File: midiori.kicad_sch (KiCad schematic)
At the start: 85 parts, among them J1 midiori-rescue_x68000_expansi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, J2 Conn_ARM_JTAG_SWD_10, J3 AudioJack3, J4 Mini-DIN-5, J5 AudioJack3, J6 AudioJack3, J7 Conn_01x06, J8 AudioJack3, J9 Mini-DIN-5, U1 74LCX07, U10 ICE40HX1K-TQ144, U11 AP2205K-3.3, U12 AK4432, U13 TL074, U14 AP2205K-3.3, U15 TL072, U16 74LCX07, U17 H11L1, U18 SN74LVC245APW, U2 AT25SF081-SSHD-X, U3 AP2127K-1.2, U4 SN74LVC245APW, U5 SN74LVC245APW, U6 SN74LVC245APW, U7 SN74LVC245APW, U8 SN74LVC245APW, U9 SN74LVC245APW, X1 16MHz, X2 24.576MHz

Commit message: drc fixes
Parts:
- H1, H2: value MountingHole -> MountingHole_Pad; symbol Mechanical:MountingHole -> Mechanical:MountingHole_Pad
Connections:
- net GND: now also H1.1, H2.1
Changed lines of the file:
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@@
 	)
 	(symbol
-		(lib_id "Mechanical:MountingHole")
+		(lib_id "Mechanical:MountingHole_Pad")
 		(at 260.35 254 0)
 		(unit 1)
-		(exclude_from_sim no)
+		(exclude_from_sim yes)
 		(in_bom no)
 		(on_board yes)
@@
 			)
 		)
-		(property "Value" "MountingHole"
-			(at 262.89 255.143 0)
+		(property "Value" "MountingHole_Pad"
+			(at 260.35 249.555 0)
 			(effects
 				(font
 					(size 1.27 1.27)
 				)
-				(justify left)
 			)
 		)
@@
 			)
 		)
-		(property "Description" ""
+		(property "Description" "Mounting Hole with connection"
 			(at 260.35 254 0)
 			(effects
@@
 			)
 		)
+		(pin "1"
+		)
 		(instances
 			(project ""
@@
 	)
 	(symbol
-		(lib_id "Mechanical:MountingHole")
+		(lib_id "Mechanical:MountingHole_Pad")
 		(at 285.75 254 0)
 		(unit 1)
-		(exclude_from_sim no)
+		(exclude_from_sim yes)
 		(in_bom no)
 		(on_board yes)
@@
 			)
 		)
-		(property "Value" "MountingHole"
-			(at 288.29 255.143 0)
+		(property "Value" "MountingHole_Pad"
+			(at 285.75 249.555 0)
 			(effects
 				(font
 					(size 1.27 1.27)
 				)
-				(justify left)
 			)
 		)
@@
 			)
 		)
-		(property "Description" ""
+		(property "Description" "Mounting Hole with connection"
 			(at 285.75 254 0)
 			(effects
@@
 			)
 		)
+		(pin "1"
+		)
 		(instances
 			(project ""
@@
 	(symbol
 		(lib_id "power:GND")
+		(at 260.35 256.54 0)
+		(unit 1)
+		(exclude_from_sim no)
+		(in_bom yes)
+		(on_board yes)
+		(dnp no)
+		(fields_autoplaced yes)
+		(property "Reference" "#PWR041"
+			(at 260.35 262.89 0)
+			(effects
+				(font
+					(size 1.27 1.27)
+				)
+				(hide yes)
+			)
+		)
+		(property "Value" "GND"
+			(at 260.35 260.6731 0)
+			(effects
+				(font
+					(size 1.27 1.27)
+				)
+			)
+		)
+		(property "Footprint" ""
+			(at 260.35 256.54 0)
+			(effects
+				(font
+					(size 1.27 1.27)
+				)
+				(hide yes)
+			)
+		)
+		(property "Datasheet" ""
+			(at 260.35 256.54 0)
+			(effects
+				(font
+					(size 1.27 1.27)
+				)
+				(hide yes)
+			)
+		)
+		(property "Description" "Power symbol creates a global label with name \"GND\" , ground"
+			(at 260.35 256.54 0)
+			(effects
+				(font
+					(size 1.27 1.27)
+				)
+				(hide yes)
+			)
+		)
+		(pin "1"
+		)
+		(instances
+			(project "midiori"
+				(path "/89a089da-4491-480f-b113-8450a227c3da"
+					(reference "#PWR041")
+					(unit 1)
+				)
+			)
+		)
+	)
+	(symbol
+		(lib_id "power:GND")
 		(at 292.1 203.2 0)
 		(unit 1)
@@
 				)
 			)
+		)
+	)
+	(symbol
+		(lib_id "power:GND")
+		(at 285.75 256.54 0)
+		(unit 1)
+		(exclude_from_sim no)
+		(in_bom yes)
+		(on_board yes)
+		(dnp no)
+		(fields_autoplaced yes)
+		(property "Reference" "#PWR044"
+			(at 285.75 262.89 0)
+			(effects
+				(font
+					(size 1.27 1.27)
+				)
+				(hide yes)
+			)
+		)
+		(property "Value" "GND"
+			(at 285.75 260.6731 0)
+			(effects
+				(font
+					(size 1.27 1.27)
+				)
+			)
+		)
+		(property "Footprint" ""
+			(at 285.75 256.54 0)
+			(effects
+				(font
+					(size 1.27 1.27)
+				)
+				(hide yes)
+			)
+		)
+		(property "Datasheet" ""
+			(at 285.75 256.54 0)
+			(effects
+				(font
+					(size 1.27 1.27)
+				)
+				(hide yes)
+			)
+		)
+		(property "Description" "Power symbol creates a global label with name \"GND\" , ground"
+			(at 285.75 256.54 0)
+			(effects
+				(font
+					(size 1.27 1.27)
+				)
+				(hide yes)
+			)
+		)
+		(pin "1"
+		)
+		(instances
+			(project "midiori"
+				(path "/89a089da-4491-480f-b113-8450a227c3da"
+					(reference "#PWR044")
+					(unit 1)
+				)
+			)

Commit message: some extra test pads
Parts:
- added C15, C38, C39: 0.1uF, Capacitor_SMD:C_0805_2012Metric, symbol Device:C
- added R17: 10k, Resistor_SMD:R_0805_2012Metric, symbol Device:R
- added TP1, TP2: TestPoint, TestPoint:TestPoint_THTPad_1.0x1.0mm_Drill0.5mm, symbol Connector:TestPoint
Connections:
- net +3V3: now also C15.1, C38.1, C39.1, R17.1
- net GND: now also C15.2, C38.2, C39.2
- net data_dir: now also R17.2
- net CBSEL0: now reaches U10.63 (IOB_42_CBSEL0)
- net CBSEL0: now also TP1.1
- net CBSEL1: now reaches U10.64 (IOB_43_CBSEL1)
- net CBSEL1: now also TP2.1
- no-connect marks 52 -> 50

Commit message: v3.0
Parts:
- J1, TP1, TP2: now left out of the parts list
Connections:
- net at J8.T, J9.5: now also U17.2; no longer R15.2
- net at J8.R, J9.4: now also R15.2; no longer U17.2
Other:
- moved on the sheet: J8
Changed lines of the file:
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@@
 	)
 	(junction
+		(at 379.73 34.29)
+		(diameter 0)
+		(color 0 0 0 0)
+	)
+	(junction
 		(at 386.08 146.05)
 		(diameter 0)
@@
 	)
 	(junction
-		(at 377.19 36.83)
+		(at 275.59 104.14)
 		(diameter 0)
 		(color 0 0 0 0)
 	)
 	(junction
-		(at 275.59 104.14)
+		(at 381 36.83)
 		(diameter 0)
 		(color 0 0 0 0)
@@
 	)
 	(junction
-		(at 373.38 39.37)
-		(diameter 0)
-		(color 0 0 0 0)
-	)
-	(junction
 		(at 285.75 26.67)
 		(diameter 0)
@@
 	)
 	(no_connect
-		(at 377.19 41.91)
+		(at 383.54 39.37)
 	)
 	(no_connect
@@
 	(wire
 		(pts
+			(xy 377.19 36.83) (xy 381 36.83)
+		)
+		(stroke
+			(width 0)
+			(type default)
+		)
+	)
+	(wire
+		(pts
 			(xy 234.95 200.66) (xy 234.95 196.85)
 		)
@@
 	(wire
 		(pts
-			(xy 31.75 128.27) (xy 31.75 130.81)
+			(xy 374.65 27.94) (xy 374.65 21.59)
 		)
 		(stroke
@@
 	(wire
 		(pts
-			(xy 205.74 53.34) (xy 208.28 53.34)
+			(xy 31.75 128.27) (xy 31.75 130.81)
 		)
 		(stroke
@@
 	(wire
 		(pts
-			(xy 290.83 140.97) (xy 290.83 133.35)
+			(xy 205.74 53.34) (xy 208.28 53.34)
 		)
 		(stroke
@@
 	(wire
 		(pts
-			(xy 226.06 118.11) (xy 228.6 118.11)
+			(xy 290.83 140.97) (xy 290.83 133.35)
 		)
 		(stroke
@@
 	(wire
 		(pts
-			(xy 370.84 39.37) (xy 373.38 39.37)
+			(xy 226.06 118.11) (xy 228.6 118.11)
 		)
 		(stroke
@@
 	(wire
 		(pts
-			(xy 393.7 21.59) (xy 405.13 21.59)
-		)
-		(stroke
-			(width 0)
-			(type default)
-		)
-	)
-	(wire
-		(pts
 			(xy 233.68 26.67) (xy 245.11 26.67)
 		)
@@
 	(wire
 		(pts
+			(xy 383.54 34.29) (xy 379.73 34.29)
+		)
+		(stroke
+			(width 0)
+			(type default)
+		)
+	)
+	(wire
+		(pts
 			(xy 153.67 58.42) (xy 153.67 36.83)
 		)
@@
 	(wire
 		(pts
+			(xy 374.65 21.59) (xy 378.46 21.59)
+		)
+		(stroke
+			(width 0)
+			(type default)
+		)
+	)
+	(wire
+		(pts
 			(xy 248.92 212.09) (xy 234.95 212.09)
 		)
@@
 	(wire
 		(pts
+			(xy 379.73 34.29) (xy 379.73 27.94)
+		)
+		(stroke
+			(width 0)
+			(type default)
+		)
+	)
+	(wire
+		(pts
 			(xy 275.59 140.97) (xy 290.83 140.97)
 		)
@@
 	(wire
 		(pts
+			(xy 407.67 21.59) (xy 407.67 48.26)
+		)
+		(stroke
+			(width 0)
+			(type default)
+		)
+	)
+	(wire
+		(pts
 			(xy 118.11 30.48) (xy 118.11 27.94)
 		)
@@
 	(wire
 		(pts
-			(xy 405.13 49.53) (xy 373.38 49.53)
-		)
-		(stroke
-			(width 0)
-			(type default)
-		)
-	)
-	(wire
-		(pts
 			(xy 87.63 129.54) (xy 92.71 129.54)
 		)
@@
 	(wire
 		(pts
-			(xy 377.19 21.59) (xy 378.46 21.59)
+			(xy 349.25 200.66) (xy 349.25 185.42)
 		)
 		(stroke
@@
 	(wire
 		(pts
-			(xy 349.25 200.66) (xy 349.25 185.42)
+			(xy 379.73 34.29) (xy 379.73 39.37)
 		)
 		(stroke
@@
 	(wire
 		(pts
+			(xy 407.67 48.26) (xy 381 48.26)
+		)
+		(stroke
+			(width 0)
+			(type default)
+		)
+	)
+	(wire
+		(pts
 			(xy 308.61 198.12) (xy 313.69 198.12)
 		)
@@
 	(wire
 		(pts
+			(xy 381 36.83) (xy 383.54 36.83)
+		)
+		(stroke
+			(width 0)
+			(type default)
+		)
+	)
+	(wire
+		(pts
 			(xy 256.54 19.05) (xy 267.97 19.05)
 		)
@@
 	(wire
 		(pts
+			(xy 379.73 27.94) (xy 374.65 27.94)
+		)
+		(stroke
+			(width 0)
+			(type default)
+		)
+	)
+	(wire
+		(pts
 			(xy 25.4 87.63) (xy 25.4 85.09)
 		)
@@
 	(wire
 		(pts
-			(xy 373.38 39.37) (xy 377.19 39.37)
+			(xy 370.84 39.37) (xy 379.73 39.37)
 		)
 		(stroke
@@
 	(wire
 		(pts
-			(xy 295.91 123.19) (xy 280.67 123.19)
+			(xy 393.7 21.59) (xy 407.67 21.59)
 		)
 		(stroke
@@
 	(wire
 		(pts
-			(xy 195.58 240.03) (xy 200.66 240.03)
+			(xy 295.91 123.19) (xy 280.67 123.19)
 		)
 		(stroke
@@
 	(wire
 		(pts
-			(xy 151.13 53.34) (xy 151.13 34.29)
+			(xy 195.58 240.03) (xy 200.66 240.03)
 		)
 		(stroke
@@
 	(wire
 		(pts
-			(xy 351.79 58.42) (xy 360.68 58.42)
+			(xy 151.13 53.34) (xy 151.13 34.29)
 		)
 		(stroke
@@
 	(wire
 		(pts
-			(xy 403.86 205.74) (xy 396.24 205.74)
+			(xy 351.79 58.42) (xy 360.68 58.42)
 		)
 		(stroke
@@
 	(wire
 		(pts
-			(xy 360.68 146.05) (xy 360.68 156.21)
+			(xy 403.86 205.74) (xy 396.24 205.74)
 		)
 		(stroke
@@
 	(wire
 		(pts
-			(xy 405.13 21.59) (xy 405.13 49.53)
+			(xy 360.68 146.05) (xy 360.68 156.21)
 		)
 		(stroke
@@
 	(wire
 		(pts
-			(xy 377.19 36.83) (xy 377.19 21.59)
-		)
-		(stroke
-			(width 0)
-			(type default)
-		)
-	)
-	(wire
-		(pts
 			(xy 168.91 247.65) (xy 168.91 256.54)
 		)
@@
 	(wire
 		(pts
+			(xy 381 36.83) (xy 381 48.26)
+		)
+		(stroke
+			(width 0)
+			(type default)
+		)
+	)
+	(wire
+		(pts
 			(xy 281.94 53.34) (xy 293.37 53.34)
 		)
@@
 	(wire
 		(pts
-			(xy 373.38 39.37) (xy 373.38 49.53)
-		)
-		(stroke
-			(width 0)
-			(type default)
-		)
-	)
-	(wire
-		(pts
 			(xy 146.05 240.03) (xy 148.59 240.03)
 		)
@@
 		(unit 1)
 		(exclude_from_sim no)
-		(in_bom yes)
+		(in_bom no)
 		(on_board yes)
 		(dnp no)
@@
 		(unit 1)
 		(exclude_from_sim no)
-		(in_bom yes)
+		(in_bom no)
 		(on_board yes)
 		(dnp no)
@@
 		(unit 1)
 		(exclude_from_sim no)
-		(in_bom yes)
+		(in_bom no)
 		(on_board yes)
 		(dnp no)
@@
 	(symbol
 		(lib_id "Connector_Audio:AudioJack3")
-		(at 382.27 39.37 180)
+		(at 388.62 36.83 180)
 		(unit 1)
 		(exclude_from_sim no)
@@
 		(fields_autoplaced yes)
 		(property "Reference" "J8"
-			(at 389.382 37.5228 0)
+			(at 395.732 34.9828 0)
 			(effects
 				(font
@@
 		)
 		(property "Value" "AudioJack3"
-			(at 389.382 39.9471 0)
+			(at 395.732 37.4071 0)
 			(effects
 				(font
@@
 		)
 		(property "Footprint" "Connector_Audio:Jack_3.5mm_CUI_SJ1-3533NG_Horizontal"
-			(at 382.27 39.37 0)
+			(at 388.62 36.83 0)
 			(effects
 				(font
@@
 		)
 		(property "Datasheet" "~"
-			(at 382.27 39.37 0)
+			(at 388.62 36.83 0)
 			(effects
 				(font
@@
 		)
 		(property "Description" "Audio Jack, 3 Poles (Stereo / TRS)"
-			(at 382.27 39.37 0)
+			(at 388.62 36.83 0)
 			(effects
 				(font

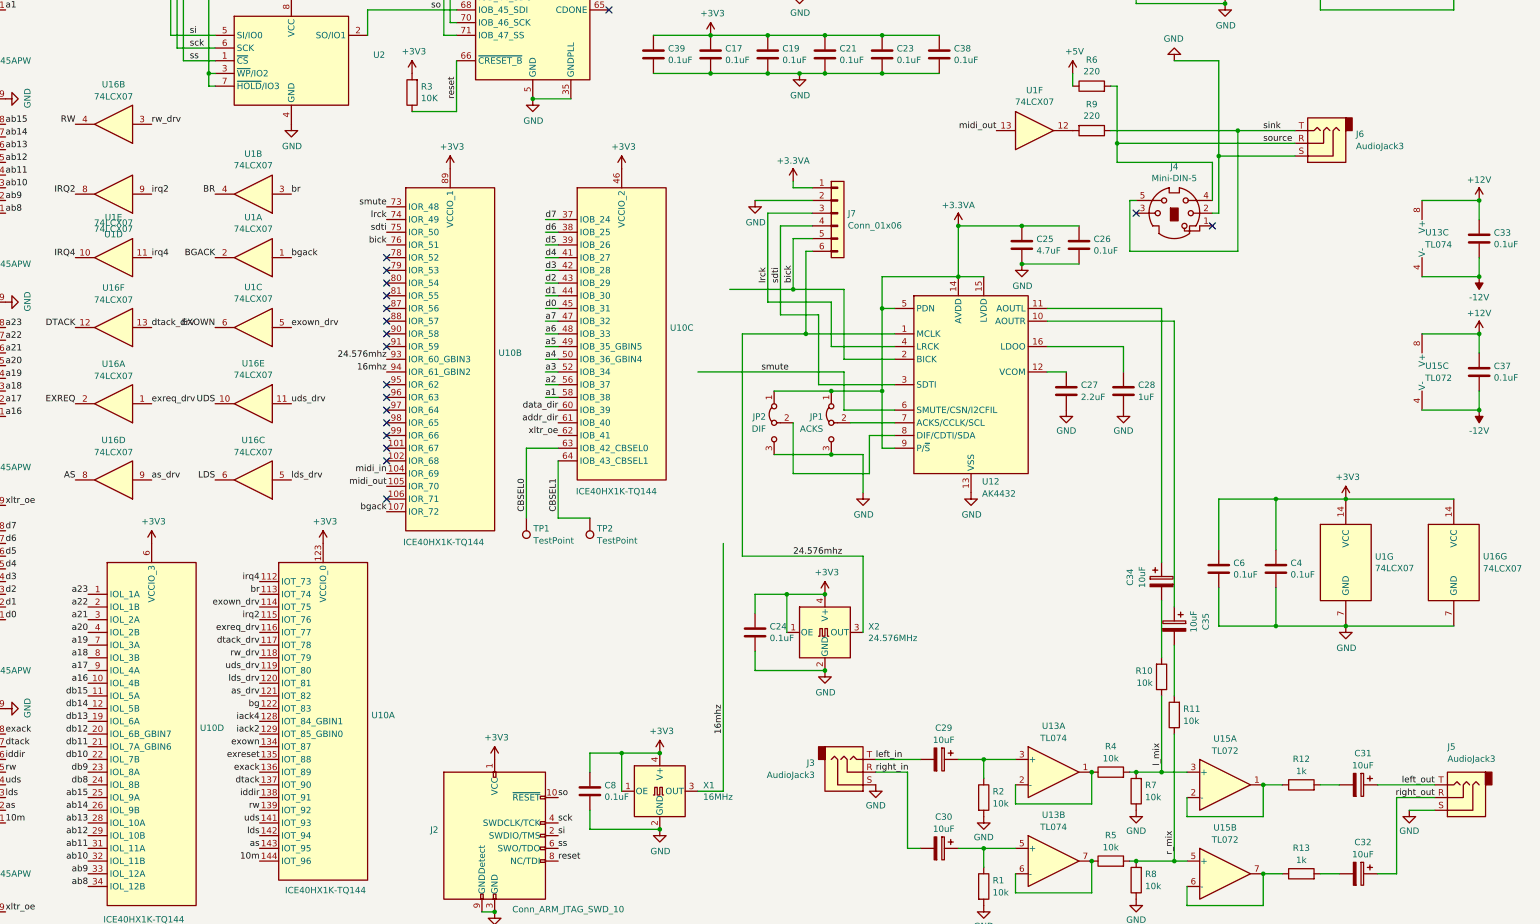
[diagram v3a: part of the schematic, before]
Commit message: add bom
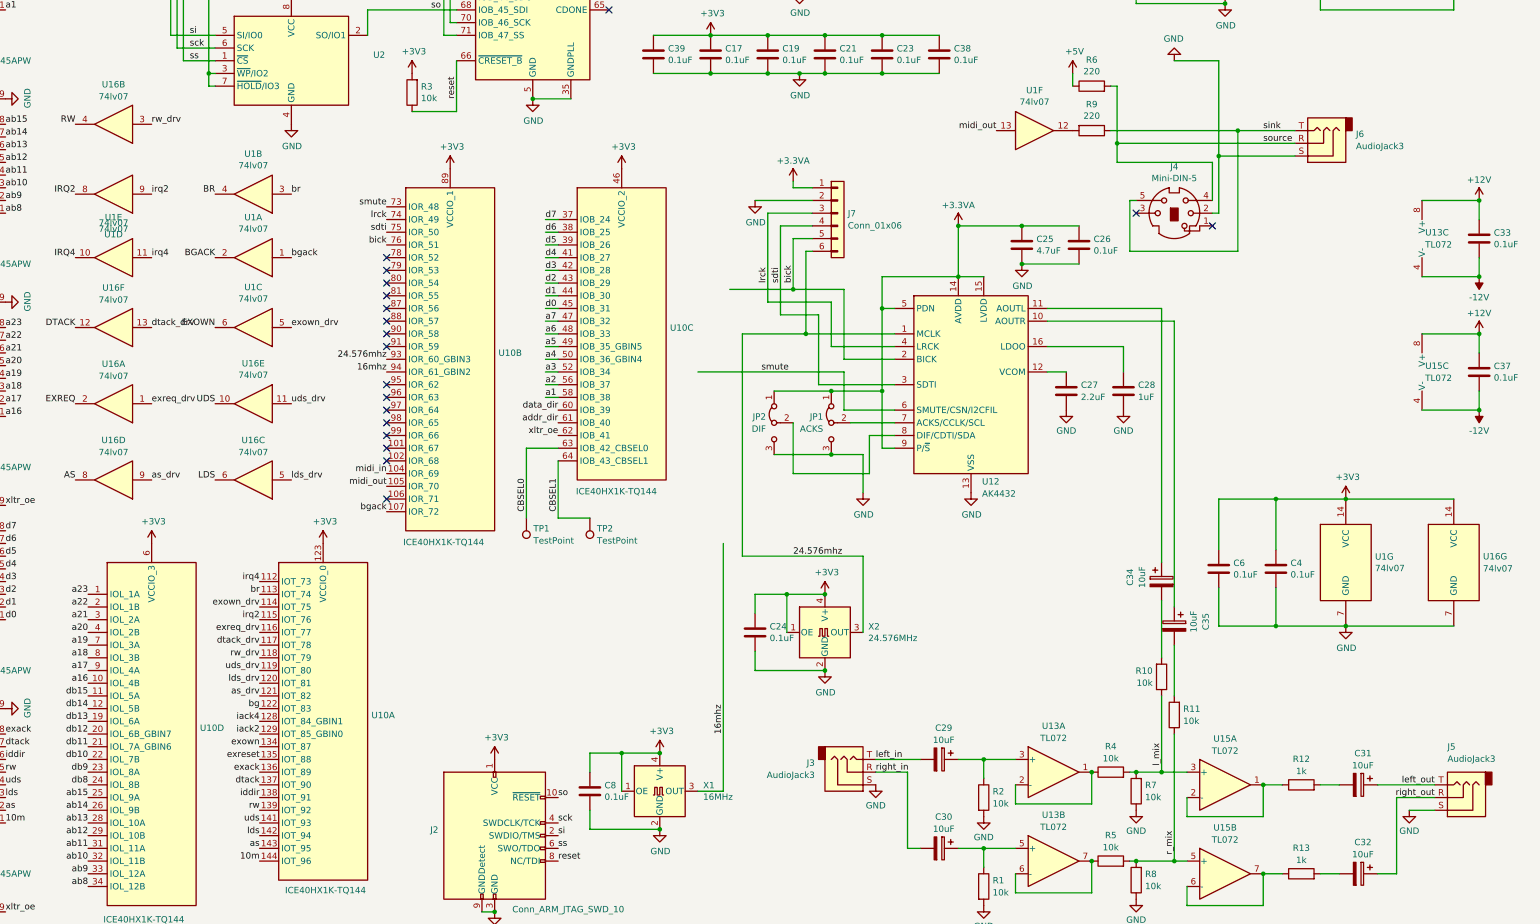
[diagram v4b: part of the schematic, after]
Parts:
- C1, C2, C25, C36: Digikey (none) -> 490-14466-1-ND
- C10, C11, C12, C13, C14, C15, C16, C17, C18, C19, C20, C21, C22, C23, C24, C26, C3, C33, C37, C38, C39, C4, C5, C6, C7, C8, C9: Digikey (none) -> 311-1140-1-ND
- C27: Digikey (none) -> 490-14467-1-ND
- C28: Digikey (none) -> 311-1365-1-ND
- J3, J5, J6, J8: Digikey (none) -> CP1-3533NG-ND
- J4, J9: Digikey (none) -> CP-2250-ND
- J7: now left out of the parts list
- R1, R10, R11, R14, R17, R2, R4, R5, R7, R8: Digikey (none) -> 311-10.0KCRCT-ND
- R12, R13: Digikey (none) -> 311-1.00KCRCT-ND
- R15, R16, R6, R9: Digikey (none) -> 311-220CRCT-ND
- R3: value 10K -> 10k; Digikey (none) -> 311-10.0KCRCT-ND
- U1, U16: value 74LCX07 -> 74lv07; Digikey (none) -> 74LV07AS14-13DICT-ND
- U10: Digikey (none) -> 220-1565-ND
- U11, U14: Digikey (none) -> AP2202K-3.3TRG1DICT-ND
- U13: value TL074 -> TL072; Digikey (none) -> 497-2200-1-ND
- U15: Digikey (none) -> 497-2200-1-ND
- U17: Digikey (none) -> H11L1SR2MCT-ND
- U2: Digikey (none) -> AT25SF081B-SSHD-B
- U3: Digikey (none) -> AP2127K-1.2TRG1DICT-ND
- X1: Digikey (none) -> 110-CB3LV-3C-16M000000CT-ND
- X2: Digikey (none) -> 110-CB3LV-3I-24M576000CT-ND

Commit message: lvc245
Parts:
- U18, U4, U5, U6, U7, U8, U9: Digikey 1727-8095-1-ND -> 1727-3104-1-ND
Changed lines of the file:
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@@
 			)
 		)
-		(property "Digikey" "1727-8095-1-ND"
+		(property "Digikey" "1727-3104-1-ND"
 			(at 105.41 35.56 0)
 			(effects
@@
 			)
 		)
-		(property "Digikey" "1727-8095-1-ND"
+		(property "Digikey" "1727-3104-1-ND"
 			(at 105.41 76.2 0)
 			(effects
@@
 			)
 		)
-		(property "Digikey" "1727-8095-1-ND"
+		(property "Digikey" "1727-3104-1-ND"
 			(at 105.41 116.84 0)
 			(effects
@@
 			)
 		)
-		(property "Digikey" "1727-8095-1-ND"
+		(property "Digikey" "1727-3104-1-ND"
 			(at 105.41 157.48 0)
 			(effects
@@
 			)
 		)
-		(property "Digikey" "1727-8095-1-ND"
+		(property "Digikey" "1727-3104-1-ND"
 			(at 105.41 198.12 0)
 			(effects
@@
 			)
 		)
-		(property "Digikey" "1727-8095-1-ND"
+		(property "Digikey" "1727-3104-1-ND"
 			(at 105.41 238.76 0)
 			(effects
@@
 			)
 		)
-		(property "Digikey" "1727-8095-1-ND"
+		(property "Digikey" "1727-3104-1-ND"
 			(at 45.72 44.45 0)
 			(effects

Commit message: add expcl/fc0/fc1/fc2, fix audio power
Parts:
- added C40, C41: 0.1uF, Capacitor_SMD:C_0805_2012Metric, symbol Device:C
- added U19: 74lv07, Package_SO:SOIC-14_3.9x8.7mm_P1.27mm, symbol 74xx:74LCX07
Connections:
- net +3.3VA: no longer J7.1 (Pin_1), JP1.1 (A), JP2.1 (A), U12.15 (LVDD), U12.5 (PDN), U12.9 (P/~{S})
- net +3V3: now also J7.1 (Pin_1), JP1.1 (A), JP2.1 (A), U12.15 (LVDD), U12.9 (P/~{S}), C40.1, C41.1, U19.14 (VCC)
- net GND: now also C40.2, C41.2, U19.11, U19.13, U19.7 (GND)
- net FC0: now reaches J1.A24 (FC0)
- net FC0: now also U19.8
- net FC1: now reaches J1.A25 (FC1)
- net FC1: now also U19.6
- net FC2: now reaches J1.A26 (FC2)
- net FC2: now also U19.4
- net EXPCL: now reaches J1.B38 (/EXPCL)
- net EXPCL: now also U19.2
- net fc0: now reaches U10.95 (IOR_62)
- net fc0: now also U19.9
- net fc1: now reaches U10.96 (IOR_63)
- net fc1: now also U19.5
- net fc2: now reaches U10.97 (IOR_64)
- net fc2: now also U19.3
- net expcl: now reaches U10.98 (IOR_65)
- net expcl: now also U19.1
- net at U10.65 (CDONE): now also U12.5 (PDN)
- no-connect marks 50 -> 43
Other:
- moved on the sheet: C1, C2, C36, C4, C6, H1, H2, U11, U14, U16G, U1G, U3
